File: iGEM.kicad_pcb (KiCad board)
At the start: 2 copper layers, 33 parts, among them IC1 TMCS1107A1BQDRQ1, IC2 TMCS1107A1BQDRQ1, IC3 MCP4642-502E_UN, J1 Conn_01x02, J2 Conn_01x02, J3 Conn_01x02, J4 Conn_01x03, Q1 TIP122, Q2 TIP122, Q3 IRF4905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

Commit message: layout draft complete
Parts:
- removed D5: P4SMF5, Diode_SMD:D_SOD-123F
- added C10: 4.7 uF, Capacitor_Tantalum_SMD:CP_EIA-3528-21_Kemet-B_Pad1.50x2.35mm_HandSolder, F.Cu at (144.5, 61.5)
- added C11: 0.1 uF, Capacitor_SMD:C_0805_2012Metric_Pad1.18x1.45mm_HandSolder, F.Cu at (159.5, 63.0)
- added C3: 0.1 uF, Capacitor_SMD:C_0805_2012Metric_Pad1.18x1.45mm_HandSolder, F.Cu at (127.5, 54.7)
- added C4: 0.1 uF, Capacitor_SMD:C_0805_2012Metric_Pad1.18x1.45mm_HandSolder, F.Cu at (133.2, 68.2)
- added C5: 0.1 uF, Capacitor_SMD:C_0805_2012Metric_Pad1.18x1.45mm_HandSolder, F.Cu at (168.8, 68.5)
- added C6: 4.7 uF, Capacitor_Tantalum_SMD:CP_EIA-3528-21_Kemet-B_Pad1.50x2.35mm_HandSolder, F.Cu at (124.5, 55.5)
- added C7: 4.7 uF, Capacitor_Tantalum_SMD:CP_EIA-3528-21_Kemet-B_Pad1.50x2.35mm_HandSolder, F.Cu at (130.2, 67.5)
- added C8: 4.7 uF, Capacitor_Tantalum_SMD:CP_EIA-3528-21_Kemet-B_Pad1.50x2.35mm_HandSolder, F.Cu at (166.0, 68.0)
- added C9: 0.1 uF, Capacitor_SMD:C_0805_2012Metric_Pad1.18x1.45mm_HandSolder, F.Cu at (145.2, 58.5)
- added H1: MH, MountingHole:MountingHole_5.3mm_M5_DIN965_Pad, F.Cu at (200.2, 92.0)
- added H2: MH, MountingHole:MountingHole_5.3mm_M5_DIN965_Pad, F.Cu at (125.2, 92.0)
- added H3: MH, MountingHole:MountingHole_5.3mm_M5_DIN965_Pad, F.Cu at (200.2, 42.0)
- added H4: MH, MountingHole:MountingHole_5.3mm_M5_DIN965_Pad, F.Cu at (125.2, 42.0)
- added HS1: Heatsink, Heatsink:Heatsink_AAVID_576802B03900G, F.Cu at (144.5, 72.8)
- added HS2: Heatsink, Heatsink:Heatsink_AAVID_576802B03900G, F.Cu at (180.5, 72.8)
- added M1: Fan, Connector_JST:JST_XH_B2B-XH-AM_1x02_P2.50mm_Vertical, F.Cu at (202.0, 51.8)
- added R10: 5K, Resistor_SMD:R_0805_2012Metric_Pad1.20x1.40mm_HandSolder, F.Cu at (145.5, 45.2)
- added R9: 5K, Resistor_SMD:R_0805_2012Metric_Pad1.20x1.40mm_HandSolder, F.Cu at (141.0, 45.2)
- C1, C2: value 10 uF -> 0.1 uF
- D3, D4: footprint Diode_THT:D_DO-201AD_P15.24mm_Horizontal -> Diode_THT:D_DO-201AD_P12.70mm_Horizontal
- moved D2 73.2 mm to (193.5, 82.7), turned to -90 degrees
- moved R6 64.2 mm to (137.5, 51.0), turned to 90 degrees
- moved IC1 63.9 mm to (134.5, 75.5), turned to 180 degrees
- moved Q3 62.6 mm to (123.2, 71.0), turned to -90 degrees
- moved R5 60.6 mm to (137.5, 55.0), turned to 90 degrees
- moved U3 60.4 mm to (132.5, 51.7), turned to 180 degrees
- moved R7 60.4 mm to (123.8, 66.5), turned to 180 degrees
- moved C1 56.0 mm to (129.2, 76.5), turned to 90 degrees
- moved J4 55.1 mm to (142.0, 40.2)
- moved IC3 53.9 mm to (161.8, 58.8), turned to 180 degrees
- moved U4 53.8 mm to (147.1, 53.5), turned to -90 degrees
- moved Q2 52.0 mm to (188.8, 82.5), turned to 180 degrees
- moved U1 51.6 mm to (136.5, 70.5)
- moved Q6 48.7 mm to (184.0, 75.3), turned to 90 degrees
- moved R1 43.9 mm to (156.0, 56.8)
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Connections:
- C1 pad 1: RHEO1_OUT -> +5V
- C2 pad 1: RHEO2_OUT -> +5V
- D3 pad 2: Net-(IC1-Pad3) -> Net-(D3-Pad2)
- D4 pad 2: Net-(IC2-Pad3) -> Net-(D4-Pad2)
- IC1 pad 1: Net-(IC1-Pad1) -> Net-(D3-Pad2)
- IC1 pad 2: Net-(IC1-Pad1) -> Net-(D3-Pad2)
- IC1 pad 3: Net-(IC1-Pad3) -> Net-(HS1-Pad1)
- IC1 pad 4: Net-(IC1-Pad3) -> Net-(HS1-Pad1)
- IC2 pad 1: Net-(IC2-Pad1) -> Net-(D4-Pad2)
- IC2 pad 2: Net-(IC2-Pad1) -> Net-(D4-Pad2)
- IC2 pad 3: Net-(IC2-Pad3) -> Net-(HS2-Pad1)
- IC2 pad 4: Net-(IC2-Pad3) -> Net-(HS2-Pad1)
- J1 pad 2: Net-(IC1-Pad3) -> Net-(D3-Pad2)
- J2 pad 2: Net-(IC2-Pad3) -> Net-(D4-Pad2)
- Q4 pad 2: Net-(IC1-Pad1) -> Net-(HS1-Pad1)
- Q6 pad 2: Net-(IC2-Pad1) -> Net-(HS2-Pad1)
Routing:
- net SDA: track 0.00 -> 104.7 mm, vias 0 -> 1
- net SCL: track 0.00 -> 96.8 mm, vias 0 -> 1
- net RHEO2_OUT: track 0.00 -> 53.0 mm
- net +5V: track 0.00 -> 48.0 mm, vias 0 -> 12
- net RHEO1_OUT: track 0.00 -> 32.3 mm
- net GND: track 0.00 -> 31.8 mm, vias 0 -> 23
- net Net-(R7-Pad1): track 0.00 -> 31.4 mm
- net Net-(R8-Pad2): track 0.00 -> 28.7 mm
- net PWM1: track 0.00 -> 14.7 mm
- net PWM2: track 0.00 -> 10.8 mm
- net Net-(Q2-Pad3): track 0.00 -> 7.64 mm
- net Net-(Q1-Pad3): track 0.00 -> 7.36 mm
- net Net-(IC1-Pad7): track 0.00 -> 7.01 mm
- net Net-(IC2-Pad7): track 0.00 -> 6.67 mm
- net RHEO2_IN: track 0.00 -> 4.85 mm
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- added copper zone on In2.Cu, net +5V
- added copper zone on In1.Cu, net GND
- added copper zone on B.Cu, net Net-(D3-Pad1)
- added copper zone on F.Cu, net Net-(D3-Pad1)
- added copper zone on B.Cu, net Net-(D3-Pad2)
- added copper zone on F.Cu, net Net-(D3-Pad2)
- added copper zone on B.Cu, net Net-(D4-Pad1)
- added copper zone on F.Cu, net Net-(D4-Pad1)
- added copper zone on B.Cu, net Net-(D4-Pad2)
- added copper zone on F.Cu, net Net-(D4-Pad2)
- added copper zone on B.Cu, net Net-(F1-Pad1)
- added copper zone on F.Cu, net Net-(F1-Pad1)
- added copper zone on B.Cu, net Net-(HS1-Pad1)
- added copper zone on F.Cu, net Net-(HS1-Pad1)
- added copper zone on B.Cu, net Net-(HS2-Pad1)
- added copper zone on F.Cu, net Net-(HS2-Pad1)
- added copper zone on B.Cu, net Net-(Q4-Pad3)
- added copper zone on F.Cu, net Net-(Q4-Pad3)
- added copper zone on B.Cu, net Net-(Q6-Pad3)
- added copper zone on F.Cu, net Net-(Q6-Pad3)
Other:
- board outline added: 85 x 60 mm
- copper layers 2 -> 4

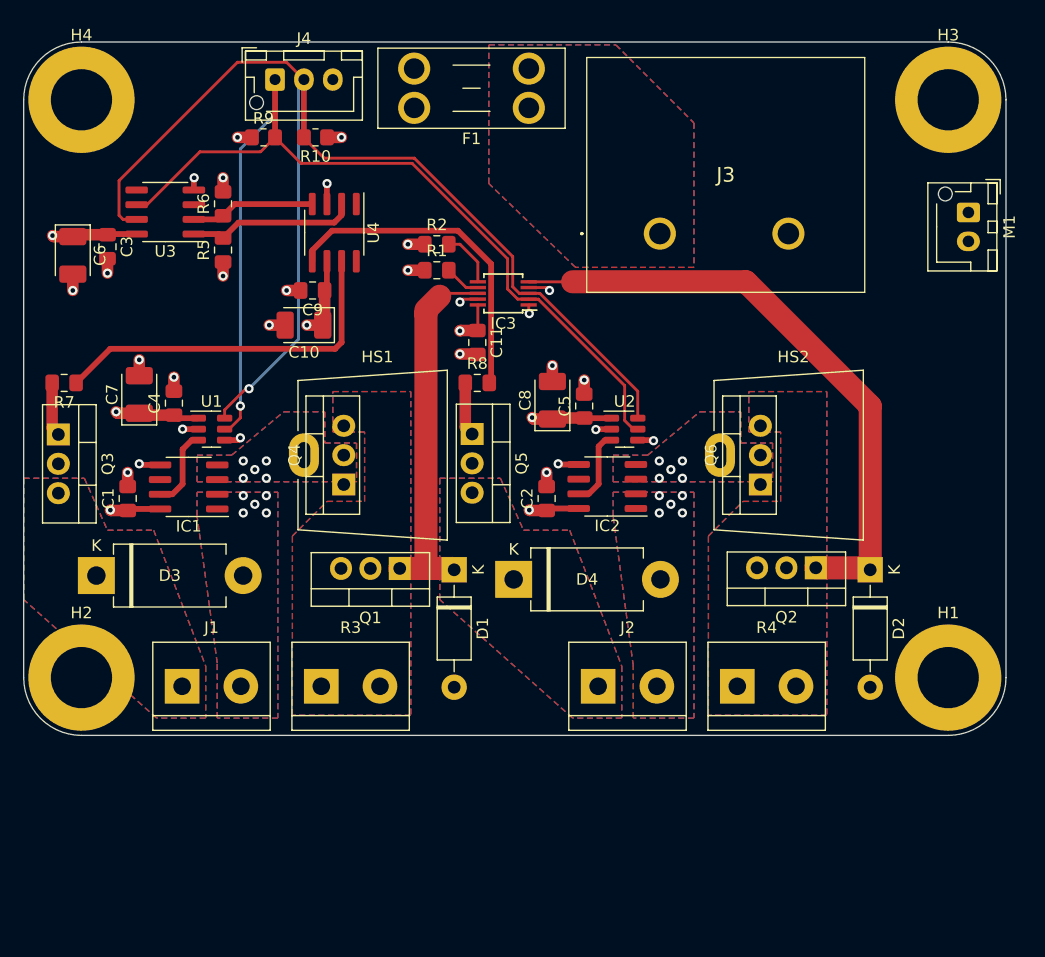
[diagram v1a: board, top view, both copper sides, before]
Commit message: cosmetic changes. added designer name
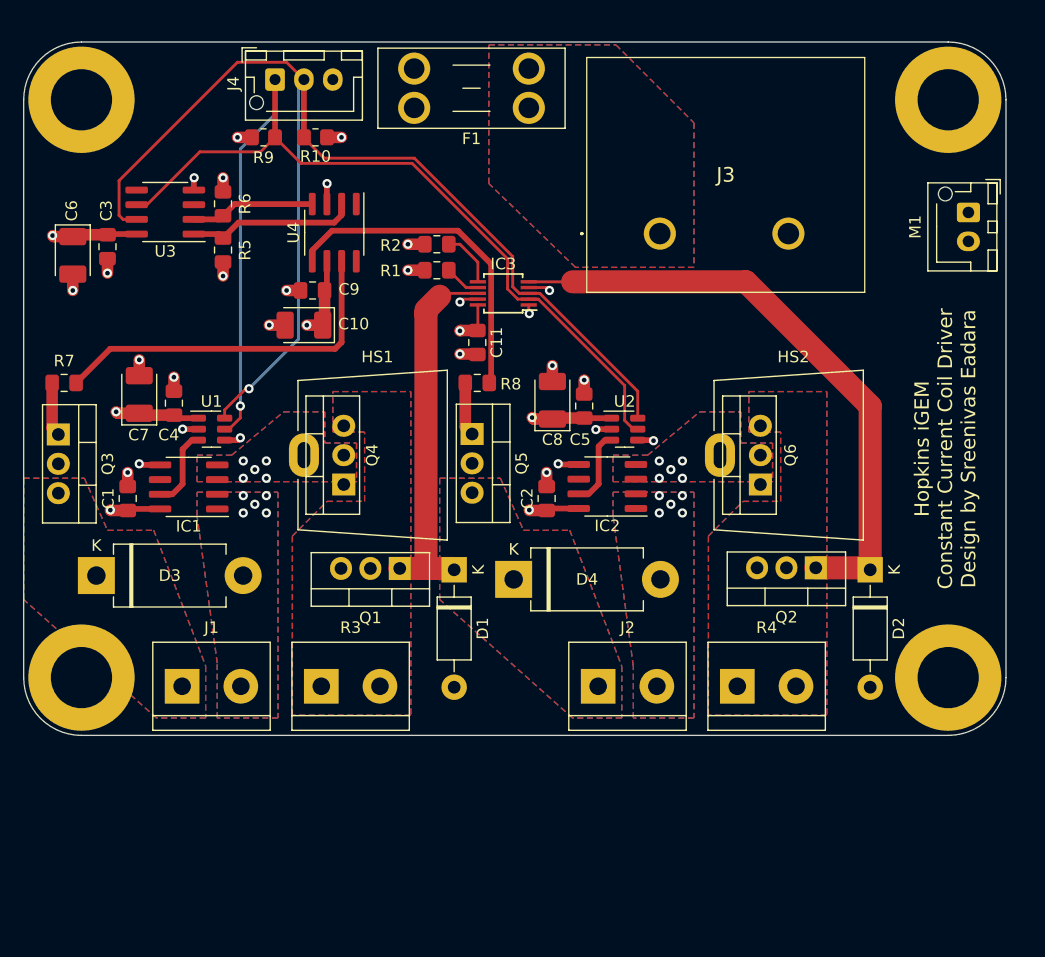
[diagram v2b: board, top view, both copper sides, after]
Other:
- board text added: "Hopkins iGEM Constant Current Coil Driver Design by Sreenivas Eadara"
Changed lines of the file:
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@@
     (property "exclude_from_bom" "")
     (attr exclude_from_pos_files exclude_from_bom)
-    (fp_text reference "H3" (at 0 -5.6) (layer "F.SilkS")
-      (effects (font (size 1 1) (thickness 0.15)))
-    )
-    (fp_text value "MH" (at 0 5.6) (layer "F.Fab")
+    (fp_text reference "H3" (at 0 -5.6) (layer "F.SilkS") hide
+      (effects (font (size 1 1) (thickness 0.15)))
+    )
+    (fp_text value "MH" (at 0 5.6) (layer "F.Fab") hide
       (effects (font (size 1 1) (thickness 0.15)))
     )
@@
     (property "Sheetname" "")
     (attr smd)
-    (fp_text reference "R6" (at 0 -1.68 90) (layer "F.SilkS")
+    (fp_text reference "R6" (at 0 1.9 90) (layer "F.SilkS")
       (effects (font (size 1 1) (thickness 0.15)))
     )
@@
     (property "Sheetname" "")
     (attr smd)
-    (fp_text reference "R2" (at 0 -1.68) (layer "F.SilkS")
+    (fp_text reference "R2" (at -4 0.1) (layer "F.SilkS")
       (effects (font (size 1 1) (thickness 0.15)))
     )
@@
     (property "Sheetname" "")
     (attr smd)
-    (fp_text reference "C4" (at 0 -1.68 90) (layer "F.SilkS")
+    (fp_text reference "C4" (at -2.75 -0.45 180) (layer "F.SilkS")
       (effects (font (size 1 1) (thickness 0.15)))
     )
@@
     (property "Sheetname" "")
     (attr through_hole)
-    (fp_text reference "M1" (at 1.25 -3.55 90) (layer "F.SilkS")
+    (fp_text reference "M1" (at 1.25 4.6 90) (layer "F.SilkS")
       (effects (font (size 1 1) (thickness 0.15)))
     )
@@
     (property "Sheetname" "")
     (attr smd)
-    (fp_text reference "R8" (at 0 -1.68) (layer "F.SilkS")
+    (fp_text reference "R8" (at 2.9 0.1) (layer "F.SilkS")
       (effects (font (size 1 1) (thickness 0.15)))
     )
@@
     (property "Sheetname" "")
     (attr smd)
-    (fp_text reference "IC3" (at 0 -2.6) (layer "F.SilkS")
+    (fp_text reference "IC3" (at 0 2.55) (layer "F.SilkS")
       (effects (font (size 1 1) (thickness 0.15)))
     )
@@
     (property "Sheetname" "")
     (attr smd)
-    (fp_text reference "C10" (at 0 -2.35) (layer "F.SilkS")
+    (fp_text reference "C10" (at -4.3 0.1) (layer "F.SilkS")
       (effects (font (size 1 1) (thickness 0.15)))
     )
@@
     (property "Sheetname" "")
     (attr smd)
-    (fp_text reference "C8" (at 0 -2.35 90) (layer "F.SilkS")
+    (fp_text reference "C8" (at -3.4 0 180) (layer "F.SilkS")
       (effects (font (size 1 1) (thickness 0.15)))
     )
@@
     (property "exclude_from_bom" "")
     (attr exclude_from_pos_files exclude_from_bom)
-    (fp_text reference "H4" (at 0 -5.6) (layer "F.SilkS")
-      (effects (font (size 1 1) (thickness 0.15)))
-    )
-    (fp_text value "MH" (at 0 5.6) (layer "F.Fab")
+    (fp_text reference "H4" (at 0 -5.6) (layer "F.SilkS") hide
+      (effects (font (size 1 1) (thickness 0.15)))
+    )
+    (fp_text value "MH" (at 0 5.6) (layer "F.Fab") hide
       (effects (font (size 1 1) (thickness 0.15)))
     )
@@
     (property "Sheetname" "")
     (attr smd)
-    (fp_text reference "R9" (at 0 -1.65) (layer "F.SilkS")
+    (fp_text reference "R9" (at 0 1.75) (layer "F.SilkS")
       (effects (font (size 1 1) (thickness 0.15)))
     )
@@
     (property "Sheetname" "")
     (attr smd)
-    (fp_text reference "R7" (at 0 -1.68) (layer "F.SilkS")
+    (fp_text reference "R7" (at 0 1.9) (layer "F.SilkS")
       (effects (font (size 1 1) (thickness 0.15)))
     )
@@
     (property "Sheetname" "")
     (attr smd)
-    (fp_text reference "U4" (at 0 -3.4 90) (layer "F.SilkS")
+    (fp_text reference "U4" (at 0 3.525 90) (layer "F.SilkS")
       (effects (font (size 1 1) (thickness 0.15)))
     )
@@
     (property "Sheetname" "")
     (attr smd)
-    (fp_text reference "R1" (at 0 -1.68) (layer "F.SilkS")
+    (fp_text reference "R1" (at -4 0.05) (layer "F.SilkS")
       (effects (font (size 1 1) (thickness 0.15)))
     )
@@
     (property "exclude_from_bom" "")
     (attr exclude_from_pos_files exclude_from_bom)
-    (fp_text reference "H2" (at 0 -5.6) (layer "F.SilkS")
-      (effects (font (size 1 1) (thickness 0.15)))
-    )
-    (fp_text value "MH" (at 0 5.6) (layer "F.Fab")
+    (fp_text reference "H2" (at 0 -5.6) (layer "F.SilkS") hide
+      (effects (font (size 1 1) (thickness 0.15)))
+    )
+    (fp_text value "MH" (at 0 5.6) (layer "F.Fab") hide
       (effects (font (size 1 1) (thickness 0.15)))
     )
@@
     (property "Sheetname" "")
     (attr through_hole)
-    (fp_text reference "Q4" (at 2.54 -4.27 90) (layer "F.SilkS")
+    (fp_text reference "Q4" (at 2.54 2.455002 90) (layer "F.SilkS")
       (effects (font (size 1 1) (thickness 0.15)))
     )
@@
     (property "Sheetname" "")
     (attr smd)
-    (fp_text reference "C7" (at 0 -2.35 90) (layer "F.SilkS")
+    (fp_text reference "C7" (at -3.5 -0.05 180) (layer "F.SilkS")
       (effects (font (size 1 1) (thickness 0.15)))
     )
@@
     (property "Sheetname" "")
     (attr smd)
-    (fp_text reference "C9" (at 0 -1.68) (layer "F.SilkS")
+    (fp_text reference "C9" (at -3.15 0.1) (layer "F.SilkS")
       (effects (font (size 1 1) (thickness 0.15)))
     )
@@
     (property "exclude_from_bom" "")
     (attr exclude_from_pos_files exclude_from_bom)
-    (fp_text reference "H1" (at 0 -5.6) (layer "F.SilkS")
-      (effects (font (size 1 1) (thickness 0.15)))
-    )
-    (fp_text value "MH" (at 0 5.6) (layer "F.Fab")
+    (fp_text reference "H1" (at 0 -5.6) (layer "F.SilkS") hide
+      (effects (font (size 1 1) (thickness 0.15)))
+    )
+    (fp_text value "MH" (at 0 5.6) (layer "F.Fab") hide
       (effects (font (size 1 1) (thickness 0.15)))
     )
@@
     (property "Sheetname" "")
     (attr smd)
-    (fp_text reference "C5" (at 0 -1.68 90) (layer "F.SilkS")
+    (fp_text reference "C5" (at -2.9 -0.35 180) (layer "F.SilkS")
       (effects (font (size 1 1) (thickness 0.15)))
     )
@@
     (property "Sheetname" "")
     (attr through_hole)
-    (fp_text reference "J4" (at 2.5 -3.55) (layer "F.SilkS")
+    (fp_text reference "J4" (at -3.6 0.35 90) (layer "F.SilkS")
       (effects (font (size 1 1) (thickness 0.15)))
     )
@@
     (property "Sheetname" "")
     (attr smd)
-    (fp_text reference "R5" (at 0 -1.68 90) (layer "F.SilkS")
+    (fp_text reference "R5" (at 0 1.9 90) (layer "F.SilkS")
       (effects (font (size 1 1) (thickness 0.15)))
     )
@@
     (property "Sheetname" "")
     (attr smd)
-    (fp_text reference "C6" (at 0 -2.35 90) (layer "F.SilkS")
+    (fp_text reference "C6" (at -3.8625 0.1 90) (layer "F.SilkS")
       (effects (font (size 1 1) (thickness 0.15)))
     )
@@
     (property "Sheetname" "")
     (attr through_hole)
-    (fp_text reference "Q6" (at 2.54 -4.27 90) (layer "F.SilkS")
+    (fp_text reference "Q6" (at 2.54 2.600001 90) (layer "F.SilkS")
       (effects (font (size 1 1) (thickness 0.15)))
     )
@@
     (property "Sheetname" "")
     (attr smd)
-    (fp_text reference "C3" (at 0 -1.68 90) (layer "F.SilkS")
+    (fp_text reference "C3" (at -3.1125 0.1 90) (layer "F.SilkS")
       (effects (font (size 1 1) (thickness 0.15)))
     )
@@
   (gr_arc (start 120.25 42) (mid 121.714466 38.464466) (end 125.25 37) (layer "Edge.Cuts") (width 0.1))
   (gr_line (start 205.25 42) (end 205.25 92) (layer "Edge.Cuts") (width 0.1))
+  (gr_text "Hopkins iGEM\nConstant Current Coil Driver\nDesign by Sreenivas Eadara" (at 200 72.2 90) (layer "F.SilkS")
+    (effects (font (size 1.25 1.25) (thickness 0.25)))
+  )
   (segment (start 155.055 82.555) (end 157.385 82.555) (width 2) (layer "F.Cu") (net 1))
   (segment (start 155.055 60.555) (end 155.055 60.445) (width 2) (layer "F.Cu") (net 1))
